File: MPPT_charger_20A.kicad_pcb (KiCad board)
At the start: 2 copper layers, 114.5 x 60.5 mm, 138 parts, among them J1 SOLAR, J2 LOAD, J3 BAT, J4 UEXT, J5 CONN_01X03, P1 CONN_01X02, P3 USB_OTG, Q1 CSD18540Q5B, Q2 CSD18540Q5B, Q3 CSD18540Q5B, Q4 CSD18540Q5B, Q5 BSS84, SW1 SW_PUSH, T1 MMBT3904, T2 MMBT3904, T4 MMBT3904, U1 LM5107, U2 STM32F072CB, U3 AZ1117, U4 LMR16006X, U5 AP2210-3.3, U6 24AA01, U7 LM358, U8 TJA1042T/3, Y1 8kHz

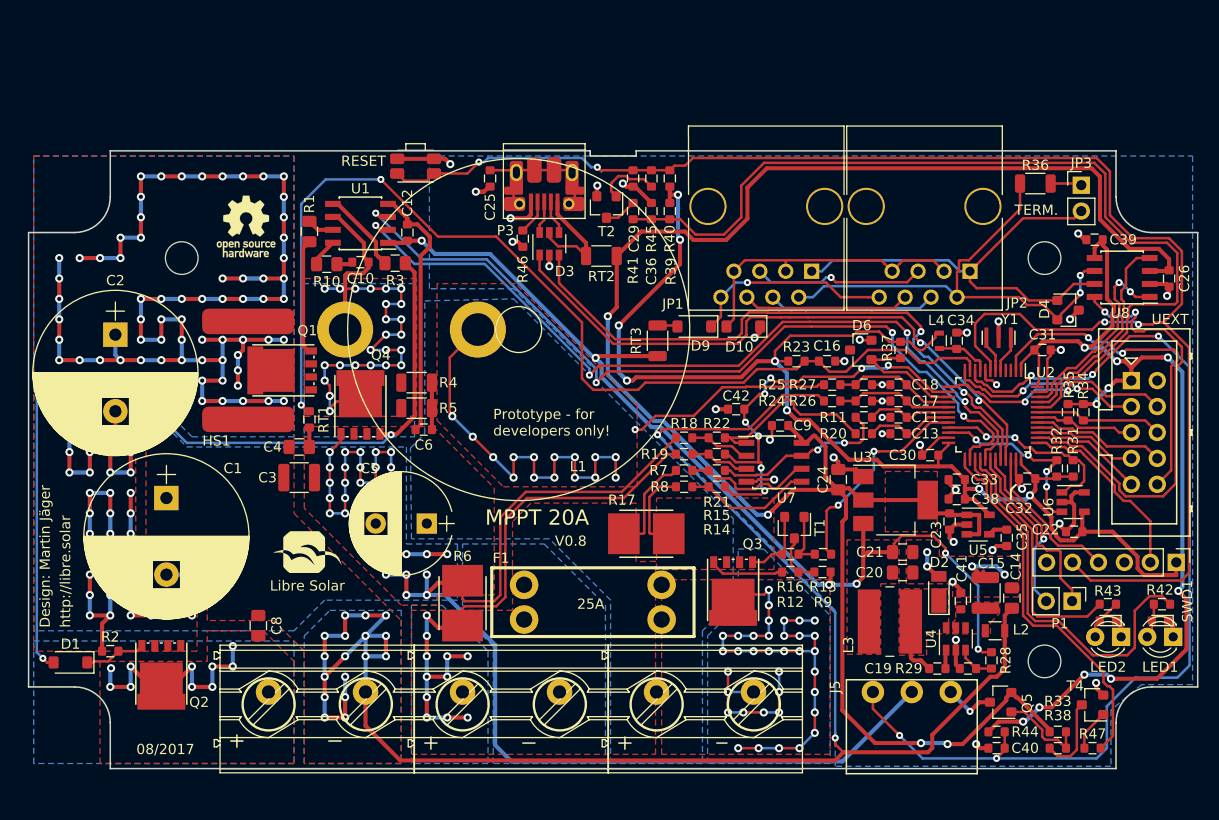
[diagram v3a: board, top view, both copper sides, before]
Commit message: V0.8.1: Small changes and update to new kicad symbol library table (nightlies only)
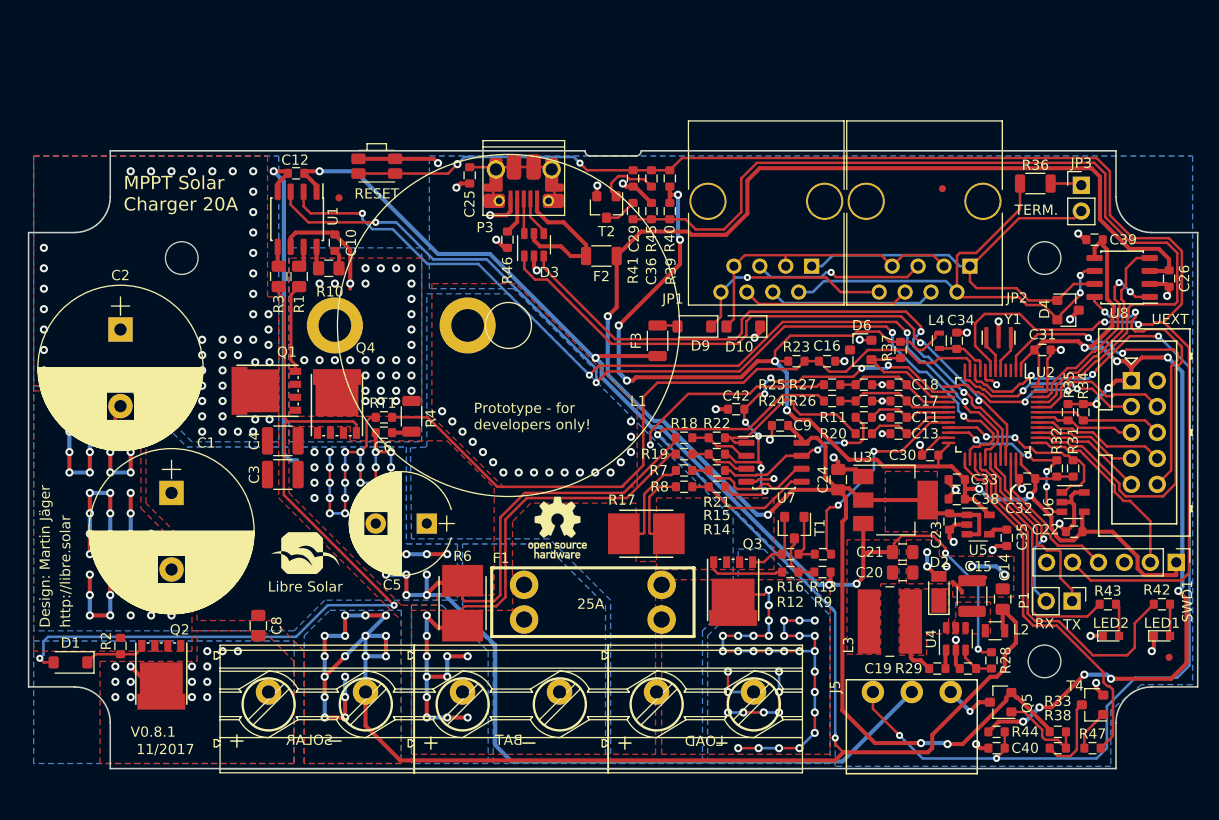
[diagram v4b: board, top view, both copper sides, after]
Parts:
- removed C41: 100n, LibreSolar:C_0603_1608
- removed HS1: Heatsink_PAD, LibreSolar:Fischer_Elektronik_FK_250_10_LF_PAK
- removed LED3, LED4: LED, LEDs:LED_0603
- removed R5: 4.7, LibreSolar:R_1206_3216
- added REF**: Fiducial_0.7mm, LibreSolar:Fiducial_0.7mm, F.Cu at (210.2, 127.1)
- added REF**: Fiducial_0.7mm, LibreSolar:Fiducial_0.7mm, F.Cu at (128.9, 82.1)
- added REF**: Fiducial_0.7mm, LibreSolar:Fiducial_0.7mm, F.Cu at (188.0, 81.2)
- C15, C3: value 2.2u -> 4.7u
- C4: value 1u -> 4.7u; footprint LibreSolar:C_0805_2012 -> LibreSolar:C_1210_3225
- LED1, LED2: footprint LEDs:LED_D3.0mm -> LEDs:LED_0603
- P3: value USB_OTG -> USB Micro B
- R4: value 4.7 -> 2.2
- U1, U8: footprint Housings_SOIC:SOIC-8_3.9x4.9mm_Pitch1.27mm -> LibreSolar:SOIC-8_3.9x4.9mm_Pitch1.27mm
- U7: value LM358 -> LM258; footprint Housings_SOIC:SOIC-8_3.9x4.9mm_Pitch1.27mm -> LibreSolar:SOIC-8_3.9x4.9mm_Pitch1.27mm
- Y1: value 8kHz -> 8MHz; footprint LibreSolar:Resonator_Murata_CSTCE -> LibreSolar:Resonator_Murata_CSTCE_G
- moved LOGO2 42.4 mm to (150.3, 114.4)
- moved C12 12.3 mm to (124.7, 79.7), turned to 180 degrees
- moved R3 11.5 mm to (123.0, 89.8), turned to 90 degrees
- moved RT1 7.30 mm to (133.3, 103.6), turned to 180 degrees
- moved U1 6.21 mm to (124.8, 84.2), turned to 270 degrees
- moved R1 4.51 mm to (125.0, 89.8)
- moved C6 3.91 mm to (133.3, 105.1)
- moved SW1 3.80 mm to (132.6, 79.0)
- moved R4 3.34 mm to (136.0, 103.5), turned to 90 degrees
- moved C10 3.14 mm to (128.5, 86.5), turned to 90 degrees
- moved Q1 2.53 mm to (121.9, 101.0)
- moved Q4 2.30 mm to (128.7, 102.4)
- moved C25 2.02 mm to (141.7, 79.9), turned to 270 degrees
- moved P3 2.02 mm to (147.0, 80.7)
- moved C4 1.71 mm to (123.4, 105.9)
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- renumbered RT2 to F2, RT3 to F3
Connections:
- C25 pad 1: GND -> Net-(C25-Pad1)
- C25 pad 2: Net-(C25-Pad2) -> GND
- P3 pad 6: Net-(C25-Pad2) -> Net-(C25-Pad1)
- Y1 pad 2: /MCU/OSC_OUT -> GND
- Y1 pad 3: GND -> /MCU/OSC_OUT
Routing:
- net /DCDC power stage/DCDC_IN: track 315.0 -> 179.5 mm, vias 88 -> 66
- net /DCDC power stage/DCDC_OUT: track 60.6 -> 20.2 mm, vias 16 -> 19
- net /DCDC power stage/SW_NODE: track 53.5 -> 13.4 mm, vias 24 -> 32
- net /Analog Frontend/TEMP_INT: track 103.2 -> 71.5 mm, vias 2 -> 0
- net /DCDC power stage/SOLAR-: track 22.8 -> 5.33 mm, vias 10 -> 15
- net GND: track 355.2 -> 341.2 mm, vias 108 -> 115
- net +10V: track 96.9 -> 110.2 mm
- net Net-(C25-Pad1): track 0.00 -> 11.0 mm
- net Net-(C25-Pad2): track 11.0 -> 0.00 mm
- net /DCDC power stage/PWM_LS: track 81.5 -> 90.1 mm
- net /DCDC power stage/PWM_HS: track 80.1 -> 87.9 mm
- net /DCDC power stage/LS_DRV: track 8.20 -> 1.94 mm
- net Net-(D3-Pad5): track 11.3 -> 14.9 mm
- net Net-(D1-Pad2): track 86.0 -> 83.0 mm
- net /MCU/LED1: track 37.9 -> 35.0 mm
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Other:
- outline, holes or cut-outs redrawn
- board text added: "+ Bat -"
- board text added: "+ Solar -"
- board text added: "- Load +"
- board text added: "11/2017"
- board text added: "MPPT Solar Charger 20A"
- board text added: "V0.8.1"
- board text removed: "- +"
- board text removed: "08/2017"
- board text removed: "MPPT 20A"
- board text removed: "V0.8"

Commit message: Bus power supply from battery instead of 10V rail
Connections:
- C5 pad 1: /DCDC power stage/DCDC_OUT -> /DCDC_OUT
- F1 pad 1: /DCDC power stage/DCDC_OUT -> /DCDC_OUT
- F3 pad 2: +10V -> /DCDC_OUT
- J2 pad 1: /DCDC power stage/DCDC_OUT -> /DCDC_OUT
- L1 pad 2: /DCDC power stage/DCDC_OUT -> /DCDC_OUT
- R25 pad 1: /DCDC power stage/DCDC_OUT -> /DCDC_OUT
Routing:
- net /DCDC_OUT: track 0.00 -> 40.0 mm, vias 0 -> 16
- net /DCDC power stage/DCDC_OUT: track 20.2 -> 0.00 mm, vias 19 -> 0
- net +10V: track 110.2 -> 104.0 mm, vias 6 -> 5
- added copper zone on B.Cu, net /DCDC_OUT
- added copper zone on F.Cu, net /DCDC_OUT
- removed copper zone on B.Cu, net /DCDC power stage/DCDC_OUT
- removed copper zone on F.Cu, net /DCDC power stage/DCDC_OUT

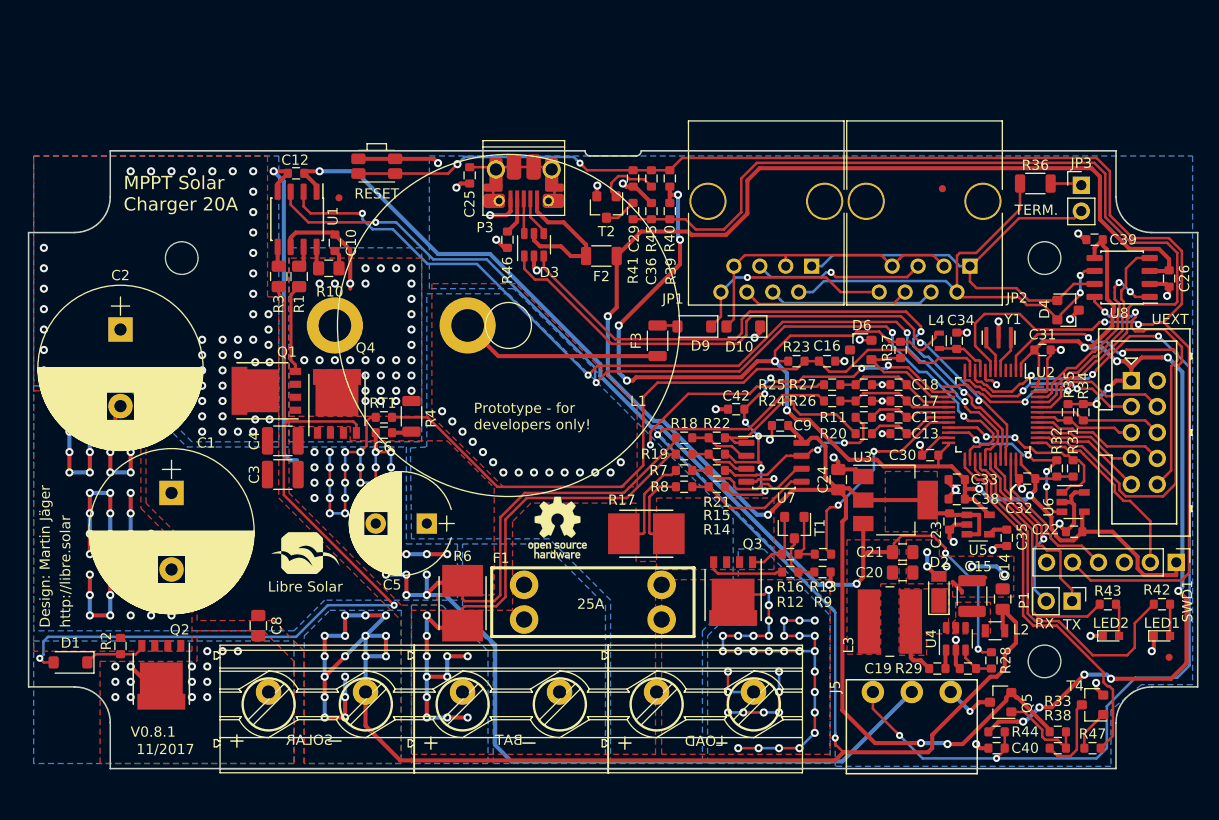
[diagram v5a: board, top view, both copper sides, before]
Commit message: Revision 0.9 for first small production batch - Switchable power supply for bus and UEXT (to be make sure to reach very low power consumption during LVD conditions) - MLCCs for EMC added to each high power input/output - Re-arrangement of some connectors after initial tests with housing
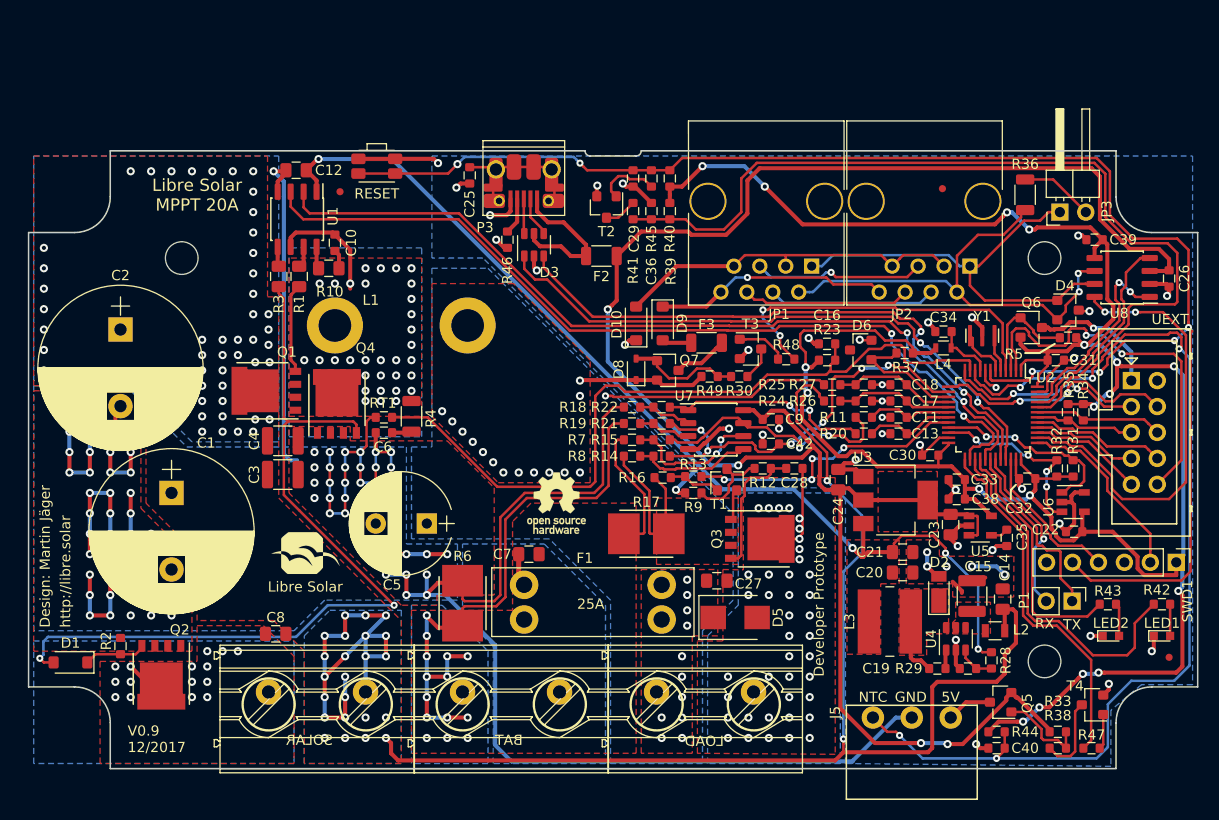
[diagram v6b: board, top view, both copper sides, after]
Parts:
- added C27: 1u, LibreSolar:C_0805_2012, F.Cu at (165.9, 119.6)
- added C28: 10n, LibreSolar:C_0603_1608, F.Cu at (173.5, 108.6)
- added C7: 1u, LibreSolar:C_0805_2012, F.Cu at (147.5, 117.0)
- added D5: SMBJ36A, LibreSolar:D_SMB, F.Cu at (167.7, 123.2)
- added D8: MM3Z12VT1G, LibreSolar:D_SOD-323, F.Cu at (158.0, 98.9)
- added Q6: BSS84, LibreSolar:SOT-23, F.Cu at (196.7, 94.8)
- added Q7: BSS84, LibreSolar:SOT-23, F.Cu at (161.1, 99.0)
- added R30: 56k, LibreSolar:R_0603_1608, F.Cu at (168.1, 99.6)
- added R48: 10k, LibreSolar:R_0603_1608, F.Cu at (172.7, 97.9)
- added R49: 56k, LibreSolar:R_0603_1608, F.Cu at (165.2, 99.6)
- added R5: 100k, LibreSolar:R_0603_1608, F.Cu at (200.3, 95.8)
- added T3: MMBT3904, LibreSolar:SOT-23, F.Cu at (169.2, 96.9)
- C11, C13, C17, C18: value 100n -> 10n
- C12, C23: footprint LibreSolar:C_0603_1608 -> LibreSolar:C_0805_2012
- JP3: footprint Pin_Headers:Pin_Header_Straight_1x02_Pitch2.54mm -> Pin_Headers:Pin_Header_Angled_1x02_Pitch2.54mm
- R11, R20, R38: value 1k -> 2.2k
- moved R9 14.8 mm to (163.6, 111.0), turned to 180 degrees
- moved R13 14.8 mm to (163.6, 109.4)
- moved R16 14.6 mm to (160.6, 109.5)
- moved D10 10.5 mm to (158.0, 94.4), turned to 90 degrees
- moved R12 10.5 mm to (170.4, 108.6), turned to 180 degrees
- moved T1 8.10 mm to (166.9, 109.7), turned to 90 degrees
- moved U7 6.54 mm to (165.8, 104.8)
- moved R14 6.18 mm to (160.5, 107.4)
- moved R15 6.18 mm to (160.5, 105.8)
- moved R21 6.18 mm to (160.5, 104.2)
- moved R22 6.18 mm to (160.5, 102.6)
- moved R18 5.92 mm to (157.6, 102.6)
- moved R19 5.92 mm to (157.6, 104.2)
- moved R7 5.92 mm to (157.6, 105.8)
- moved R8 5.92 mm to (157.6, 107.4)
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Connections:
- F3 pad 2: /DCDC_OUT -> Net-(F3-Pad2)
- J4 pad 1: +3V3 -> Net-(J4-Pad1)
- JP3 pad 1: Net-(JP3-Pad1) -> /Communication Interfaces/CAN_H
- JP3 pad 2: /Communication Interfaces/CAN_H -> Net-(JP3-Pad2)
- R36 pad 1: Net-(JP3-Pad1) -> Net-(JP3-Pad2)
- U2 pad 3: Net-(U2-Pad3) -> /Communication Interfaces/UEXT_EN
- U2 pad 4: Net-(U2-Pad4) -> /Communication Interfaces/V_BUS_EN
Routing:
- net /DCDC power stage/LOAD-: track 63.8 -> 8.14 mm, vias 36 -> 40
- net /Communication Interfaces/V_BUS_EN: track 0.00 -> 35.0 mm, vias 0 -> 2
- net /DCDC power stage/DCDC_IN: track 179.5 -> 163.8 mm, vias 66 -> 72
- net Net-(J4-Pad1): track 0.00 -> 13.2 mm, vias 0 -> 1
- net Net-(D8-Pad2): track 0.00 -> 11.1 mm
- net /Communication Interfaces/UEXT_EN: track 0.00 -> 11.0 mm
- net +3V3: track 229.8 -> 239.3 mm
- net Net-(JP3-Pad2): track 0.00 -> 7.27 mm
- net Net-(R11-Pad1): track 17.7 -> 24.9 mm
- net /DCDC power stage/~LOAD_EN: track 21.0 -> 27.8 mm, vias 2 -> 4
- net Net-(C28-Pad1): track 7.65 -> 13.3 mm
- net /Communication Interfaces/CAN_GND: track 29.2 -> 34.7 mm
- net Net-(F3-Pad2): track 0.00 -> 5.37 mm
- net /DCDC_OUT: track 40.0 -> 34.8 mm, vias 16 -> 26
- net Net-(R48-Pad1): track 0.00 -> 4.94 mm
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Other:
- board text added: "CAN bus (daisy chain)"
- board text added: "DCDC_IN"
- board text added: "DCDC_OUT"
- board text added: "Developer Prototype"
- board text added: "Libre Solar MPPT 20A"
- board text added: "MISO"
- board text added: "MOSI"
- board text added: "SCK"
- board text added: "SCL"
- board text added: "SDA"
- board text added: "SSEL"
- board text added: "SW"
- board text added: "Term. 120R"
- board text added: "USB"
- board text added: "V0.9 12/2017"
- board text added: "~RESET"
- board text removed: "11/2017"
- board text removed: "CAN"
- board text removed: "MPPT Solar Charger 20A"
- board text removed: "Prototype - for developers only!"
- board text removed: "RST"
- board text removed: "TERM."
- board text removed: "V0.8.1"

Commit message: Final version for Jan/2018 production
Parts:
- added LOGO?: LOGO-S_PLACE_M, LibreSolar:Watterott_Logo, B.Cu at (158.5, 86.6)
- added LOGO?: LOGO-S_PLACE_M, LibreSolar:Watterott_Logo, F.Cu at (103.1, 89.4)
- added REF***: WEEE-Logo_4.2x6mm_SilkScreen, Symbols:WEEE-Logo_4.2x6mm_SilkScreen, B.Cu at (150.5, 87.6)
- C12, C23: value 1u -> 2.2u; footprint LibreSolar:C_0805_2012 -> LibreSolar:C_0603_1608
- D3: value USBLC6-2SC6 -> USBLC6-2SC6Y
- LED1: value LED -> LED_red
- LED2: value LED -> LED_green
- moved LED1 5.99 mm to (204.1, 122.4)
- moved R42 5.51 mm to (204.1, 120.8)
- moved R47 5.00 mm to (202.7, 131.0)
- moved R43 4.70 mm to (204.1, 126.6)
- moved T4 3.25 mm to (202.7, 135.0), turned to 0 degrees
- moved LED2 3.22 mm to (204.1, 128.2)
- moved REF** 0.91 mm to (210.1, 126.2)
- moved C12 0.32 mm to (124.6, 79.7)
- moved Q5 0.10 mm to (193.7, 131.6), turned to 0 degrees
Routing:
- net +5V: track 187.3 -> 174.6 mm, vias 4 -> 8
- net +3V3: track 239.3 -> 228.3 mm, vias 18 -> 15
- net /MCU/LED1: track 35.0 -> 27.1 mm
- net /DCDC power stage/DCDC_IN: track 163.8 -> 157.2 mm, vias 72 -> 71
- net /DCDC power stage/SW_NODE: track 13.4 -> 17.1 mm
- net /Communication Interfaces/5V_OUT: track 4.46 -> 6.52 mm
- net /Communication Interfaces/CAN_H: track 43.3 -> 45.2 mm, vias 0 -> 1
- net +10V: track 104.3 -> 106.3 mm
- net Net-(Q5-Pad1): track 8.93 -> 10.9 mm
- net /Communication Interfaces/5V_OUT_EN: track 35.4 -> 33.6 mm
- net Net-(LED2-Pad2): track 3.22 -> 1.60 mm
- net Net-(LED1-Pad2): track 3.10 -> 1.60 mm
- net /MCU/SSEL: track 37.5 -> 36.1 mm
- net /MCU/I2C1_SDA: track 12.6 -> 13.8 mm
- net /DCDC power stage/~LOAD_EN: track 27.8 -> 26.7 mm
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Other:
- board text added: "Development Prototype!"
- board text added: "V0.10 01/2018"
- board text added: "watterott.com"
- board text removed: "Developer Prototype"
- board text removed: "V0.9 12/2017"
